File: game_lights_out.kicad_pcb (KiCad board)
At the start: 2 copper layers, 171.2 x 136.9 mm, 99 parts, among them SW1 SW_MEC_5E, SW10 SW_MEC_5E, SW11 SW_MEC_5E, SW12 SW_MEC_5E, SW13 SW_MEC_5E, SW14 SW_MEC_5E, SW15 SW_MEC_5E, SW16 SW_MEC_5E, SW17 SW_MEC_5E, SW18 SW_MEC_5E, SW19 SW_MEC_5E, SW2 SW_MEC_5E, SW20 SW_MEC_5E, SW21 SW_MEC_5E, SW22 SW_MEC_5E, SW23 SW_MEC_5E, SW24 SW_MEC_5E, SW25 SW_MEC_5E, SW26 SW_MEC_5E, SW27 SW_MEC_5E, SW28 SW_MEC_5E, SW29 SW_MEC_5E, SW3 SW_MEC_5E, SW30 SW_MEC_5E, SW31 SW_MEC_5E, SW32 SW_MEC_5E, SW33 SW_MEC_5E, SW34 SW_MEC_5E, SW35 SW_MEC_5E, SW36 SW_MEC_5E, SW37 SW_MEC_5E, SW38 SW_MEC_5E, SW39 SW_MEC_5E, SW4 SW_MEC_5E, SW40 SW_MEC_5E, SW5 SW_MEC_5E, SW6 SW_MEC_5E, SW7 SW_MEC_5E, SW8 SW_MEC_5E, SW9 SW_MEC_5E, U1 ATmega328-P, U2 ULN2803A

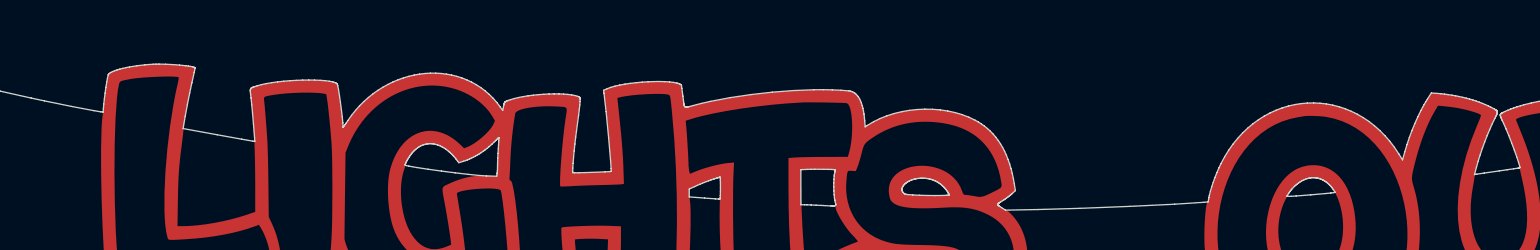
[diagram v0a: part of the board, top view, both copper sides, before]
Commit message: Removed JLCPCB batch-number placeholder
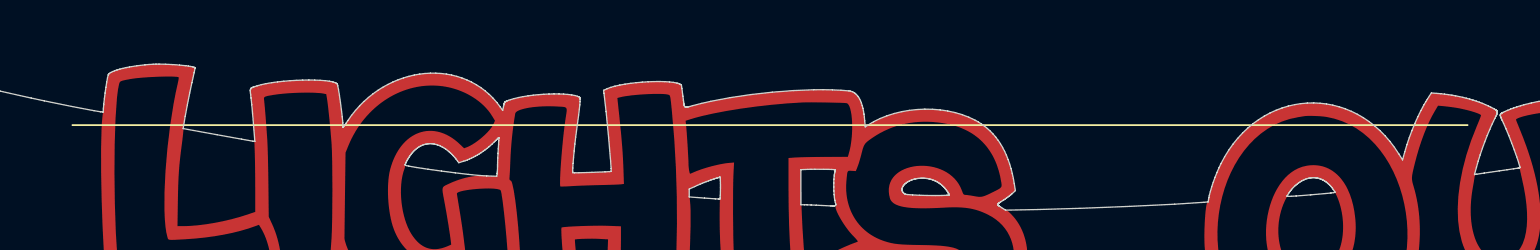
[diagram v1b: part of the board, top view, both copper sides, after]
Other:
- board text removed: "JLCJLCJLCJLC"
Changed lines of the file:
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@@
   (gr_line (start 191.141912 149.278363) (end 191.142349 149.283345)
     (stroke (width 1.5) (type solid)) (layer "F.SilkS"))
+  (gr_line (start 40.720182 32.4) (end 157.81 32.4)
+    (stroke (width 0.15) (type default)) (layer "F.SilkS"))
   (gr_line (start 53 160.587) (end 200 160.587)
     (stroke (width 0.198) (type default)) (layer "F.SilkS"))
@@
     (effects (font (size 1 1) (thickness 0.15)) (justify left bottom mirror))
   )
-  (gr_text "JLCJLCJLCJLC" (at 96.2 159.8) (layer "B.SilkS")
-    (effects (font (size 1.5 1.5) (thickness 0.3) bold) (justify left bottom mirror))
-  )
   (gr_text "MISO" (at 48.26 97.155) (layer "B.SilkS")

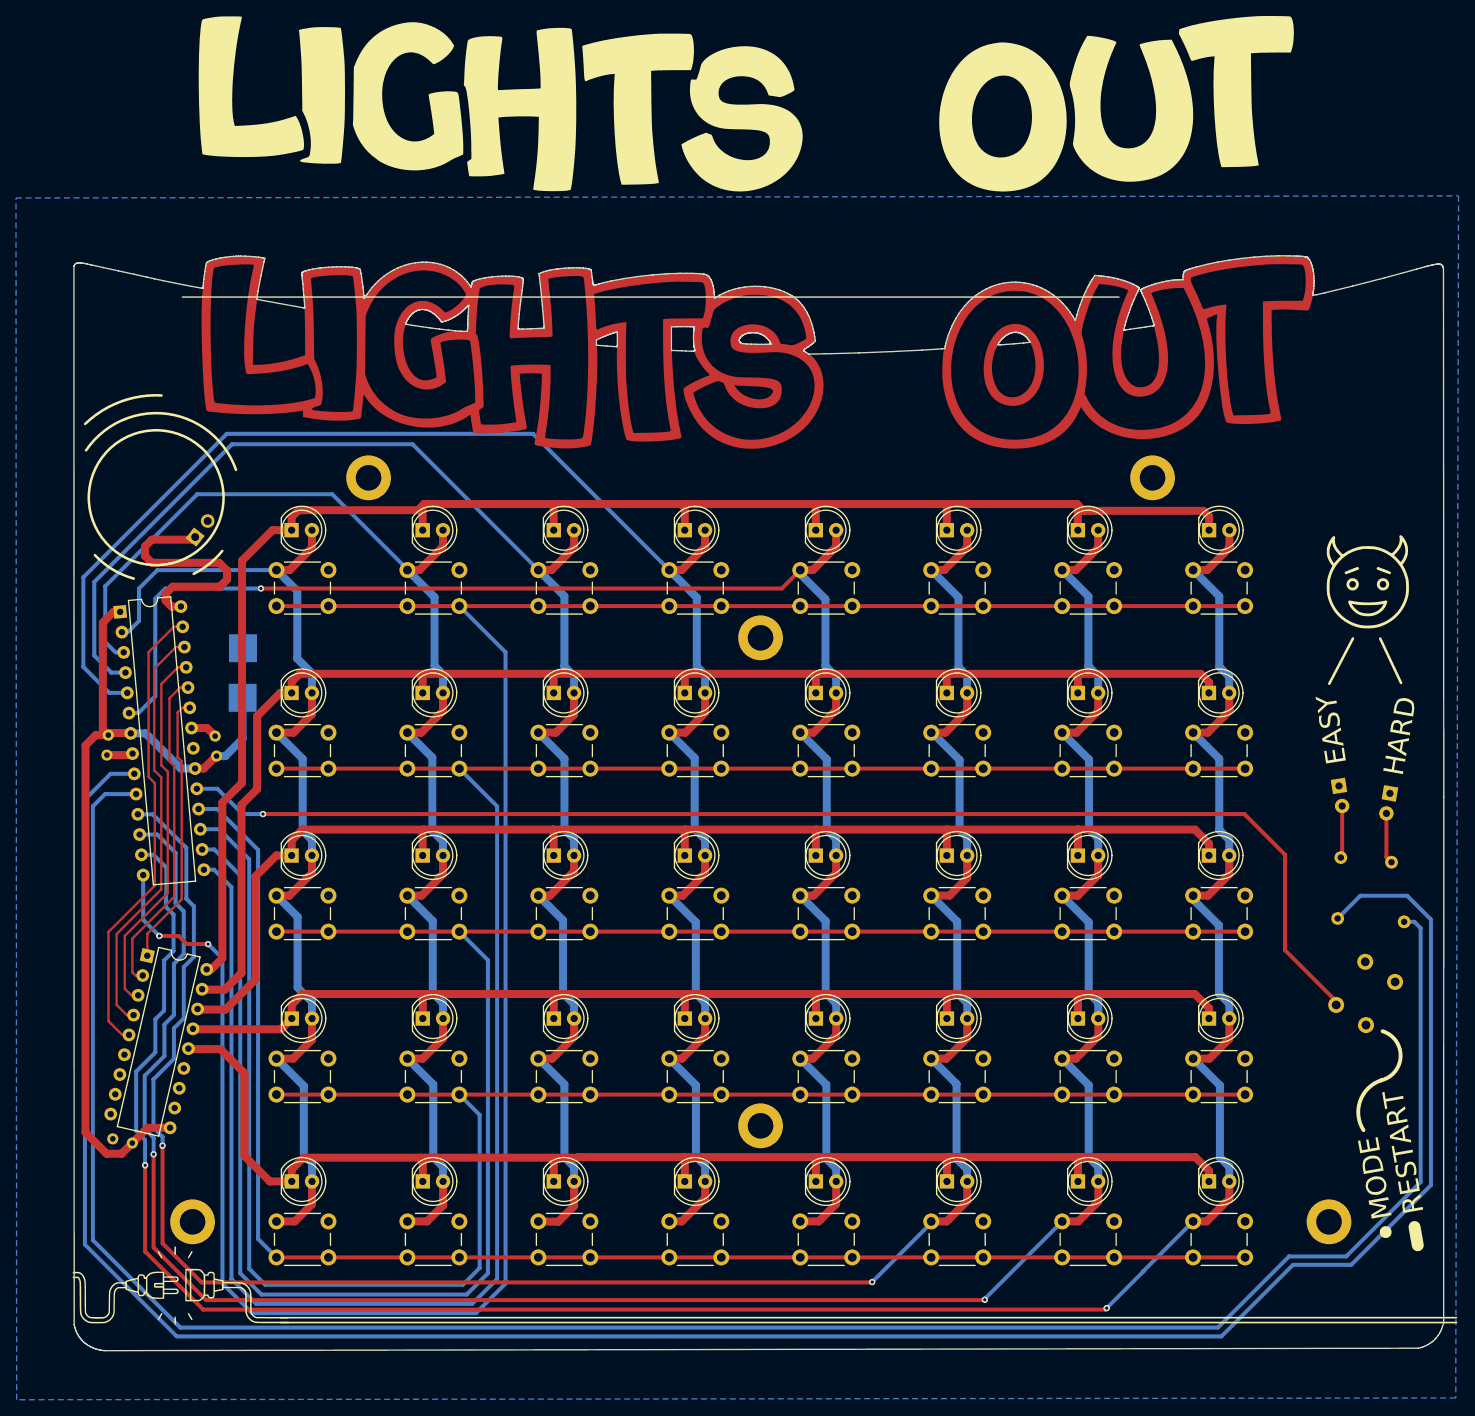
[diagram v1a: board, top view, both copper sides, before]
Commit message: Updated mounting holes
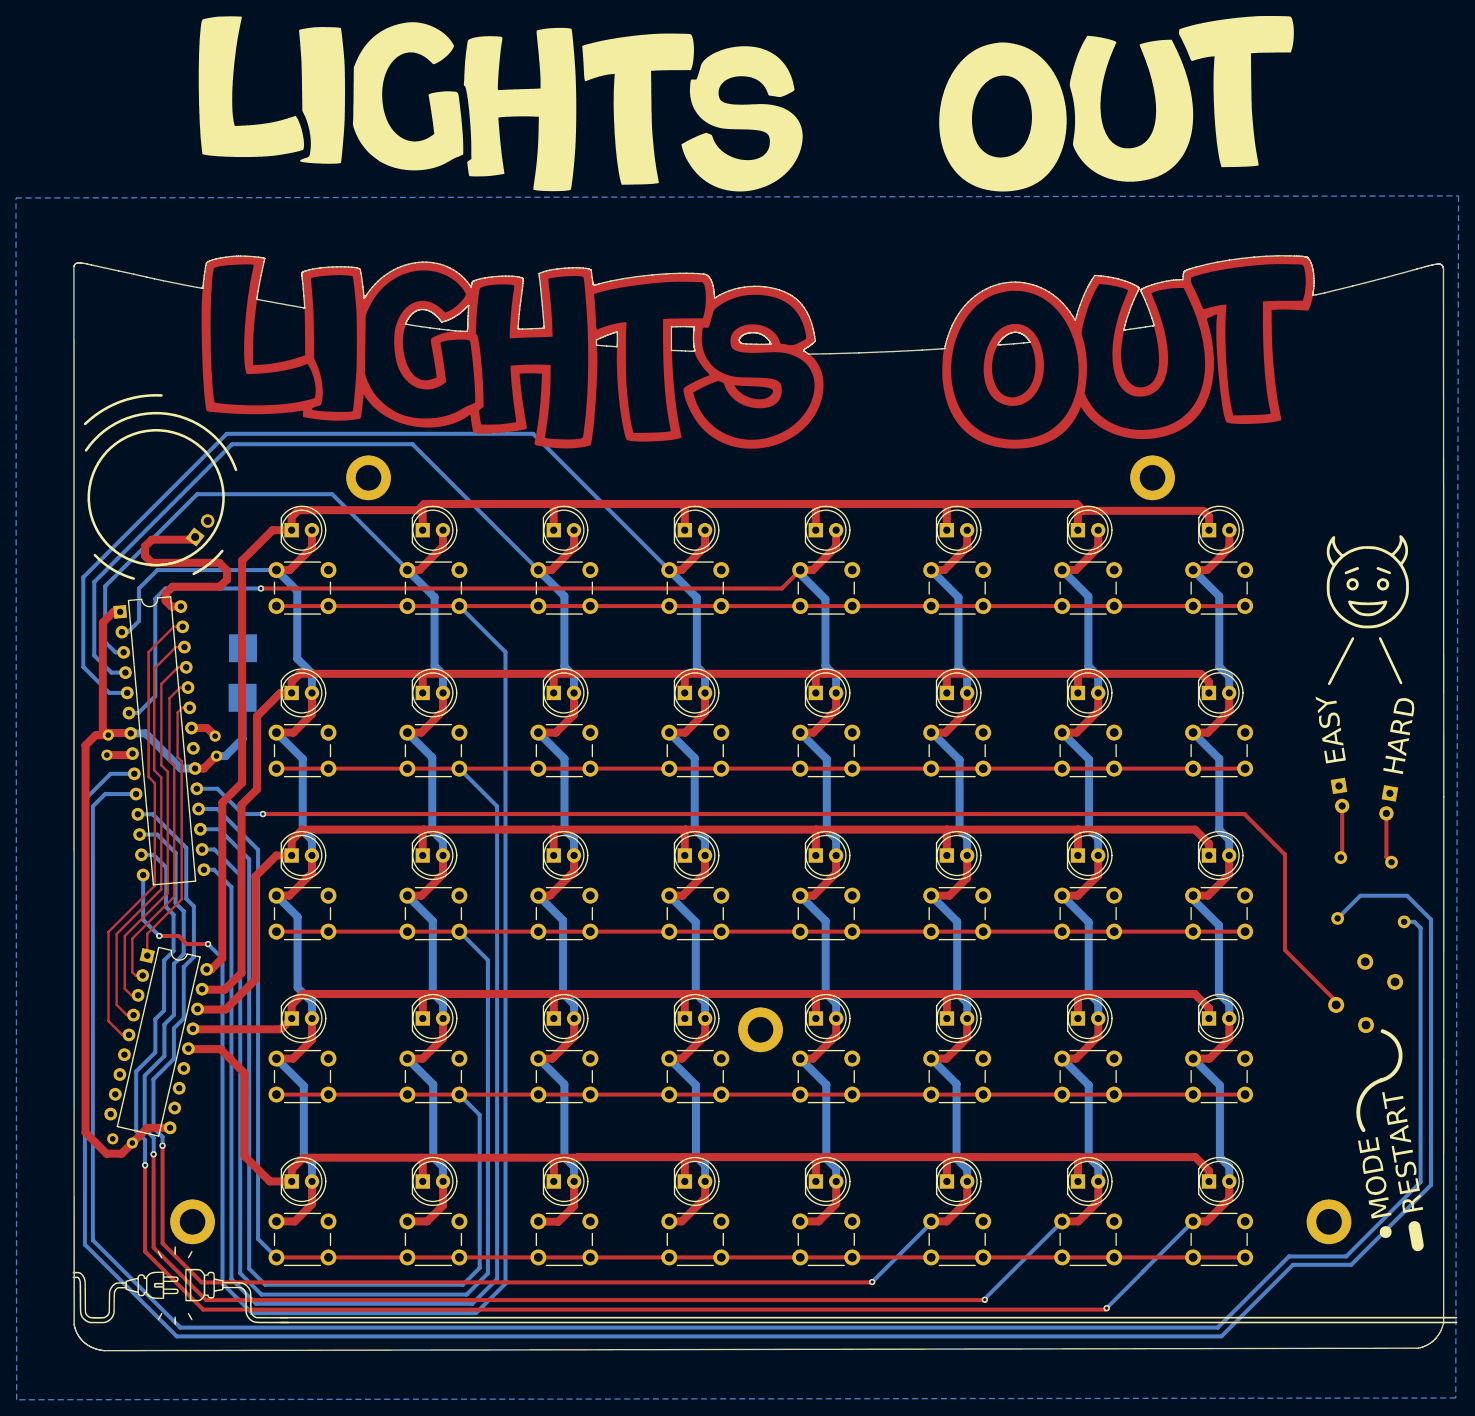
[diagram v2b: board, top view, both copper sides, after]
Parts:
- removed the REF** at (113.0, 75.0)
- moved REF** 12.0 mm to (113.0, 124.0)
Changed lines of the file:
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@@
   )
   (footprint "MountingHole:MountingHole_3.2mm_M3_DIN965_Pad" (layer "F.Cu")
-    (at 113 136)
+    (at 113 124)
     (descr "Mounting Hole 3.2mm, M3, DIN965")
     (tags "mounting hole 3.2mm m3 din965")
@@
     )
   )
-  (footprint "MountingHole:MountingHole_3.2mm_M3_DIN965_Pad" (layer "F.Cu")
-    (at 113 75)
-    (descr "Mounting Hole 3.2mm, M3, DIN965")
-    (tags "mounting hole 3.2mm m3 din965")
-    (attr exclude_from_pos_files exclude_from_bom)
-    (fp_text reference "REF**" (at 0 -3.8) (layer "F.SilkS") hide
-        (effects (font (size 1 1) (thickness 0.15)))
-    )
-    (fp_text value "MountingHole_3.2mm_M3_DIN965_Pad" (at 0 3.8) (layer "F.Fab") hide
-        (effects (font (size 1 1) (thickness 0.15)))
-    )
-    (fp_text user "${REFERENCE}" (at -0.01 -0.25) (layer "F.Fab") hide
-        (effects (font (size 1 1) (thickness 0.15)))
-    )
-    (fp_circle (center 0 0) (end 2.8 0)
-      (stroke (width 0.15) (type solid)) (fill none) (layer "Cmts.User"))
-    (fp_circle (center 0 0) (end 3.05 0)
-      (stroke (width 0.05) (type solid)) (fill none) (layer "F.CrtYd"))
-    (pad "1" thru_hole circle (at 0 0) (size 5.6 5.6) (drill 3.2) (layers "*.Cu" "*.Mask"))
-  )
   (footprint "kicad_footprints:SW_PUSH_6mm_H5mm" (layer "F.Cu")
     (at 101.594287 107.225)
@@
   (gr_line (start 191.141912 149.278363) (end 191.142349 149.283345)
     (stroke (width 1.5) (type solid)) (layer "F.SilkS"))
-  (gr_line (start 40.720182 32.4) (end 157.81 32.4)
-    (stroke (width 0.15) (type default)) (layer "F.SilkS"))
   (gr_line (start 53 160.587) (end 200 160.587)
     (stroke (width 0.198) (type default)) (layer "F.SilkS"))

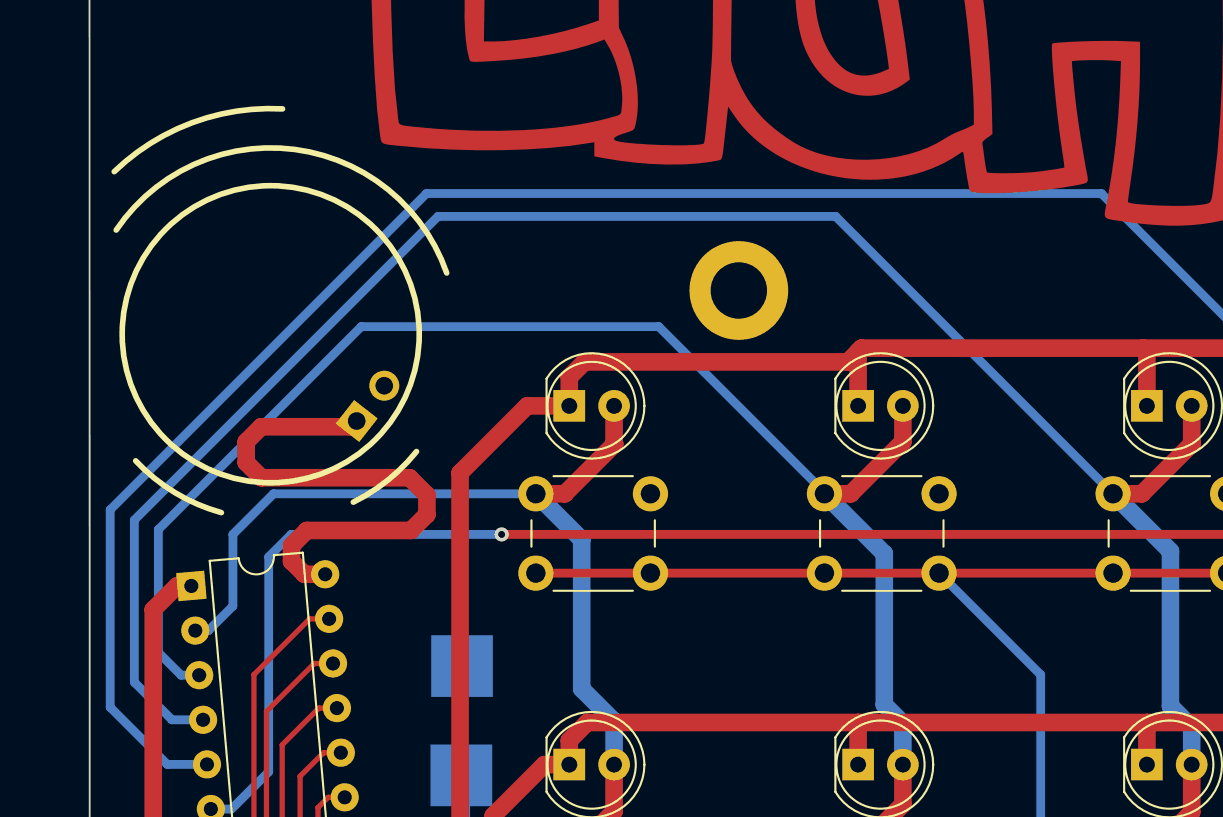
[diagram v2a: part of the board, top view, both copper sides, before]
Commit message: Updated speaker size and placement
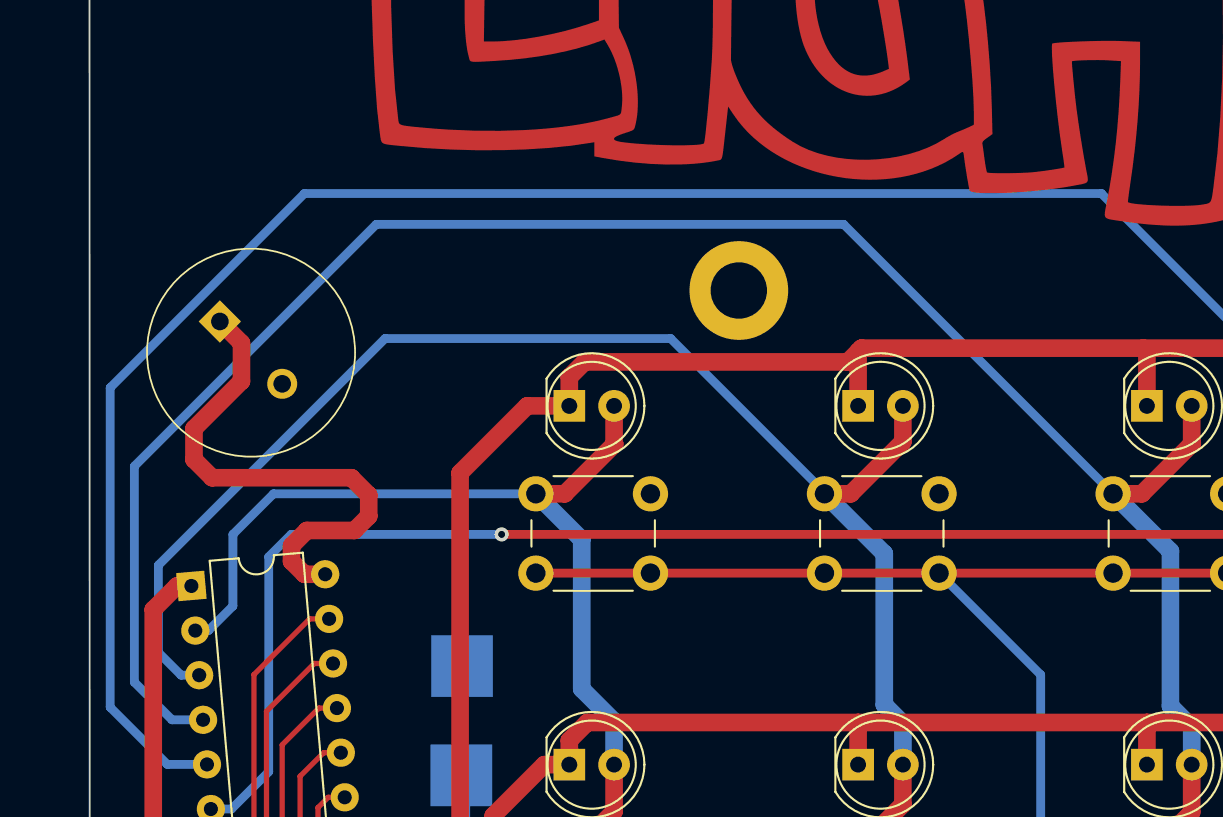
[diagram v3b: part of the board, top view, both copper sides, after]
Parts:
- moved LS1 7.14 mm to (36.3, 58.5), turned to -45 degrees
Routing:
- net C4: track 213.8 -> 217.8 mm
- net SPK: track 31.6 -> 29.3 mm
- net C2: track 164.8 -> 163.1 mm
- net C3: track 191.9 -> 193.3 mm
